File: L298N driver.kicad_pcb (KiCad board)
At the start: 2 copper layers, 155.6 x 80.8 mm, 32 parts, among them J2 Conn_01x02, J3 Conn_01x02, J6 Screw_Terminal_01x02, J8 Conn_01x02, J9 Conn_01x02, U1 L298N, U2 LM78M05_TO220, U3 DEV-15795, U4 74HC595, U5 L298N

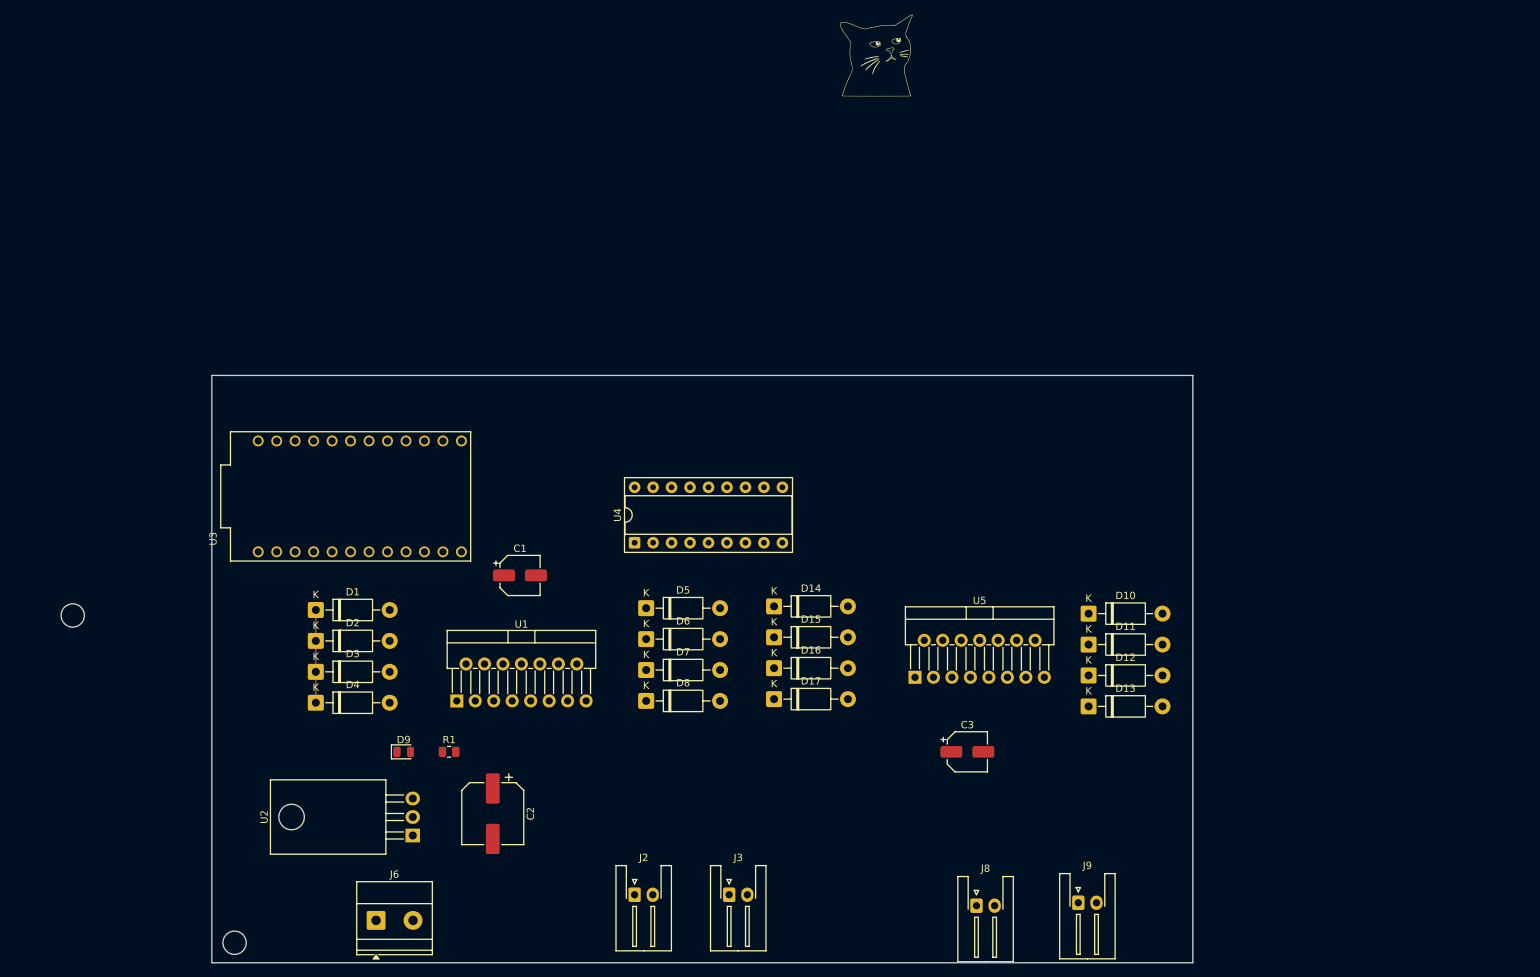
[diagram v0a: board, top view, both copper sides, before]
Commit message: changed to fast switching diode UF4004
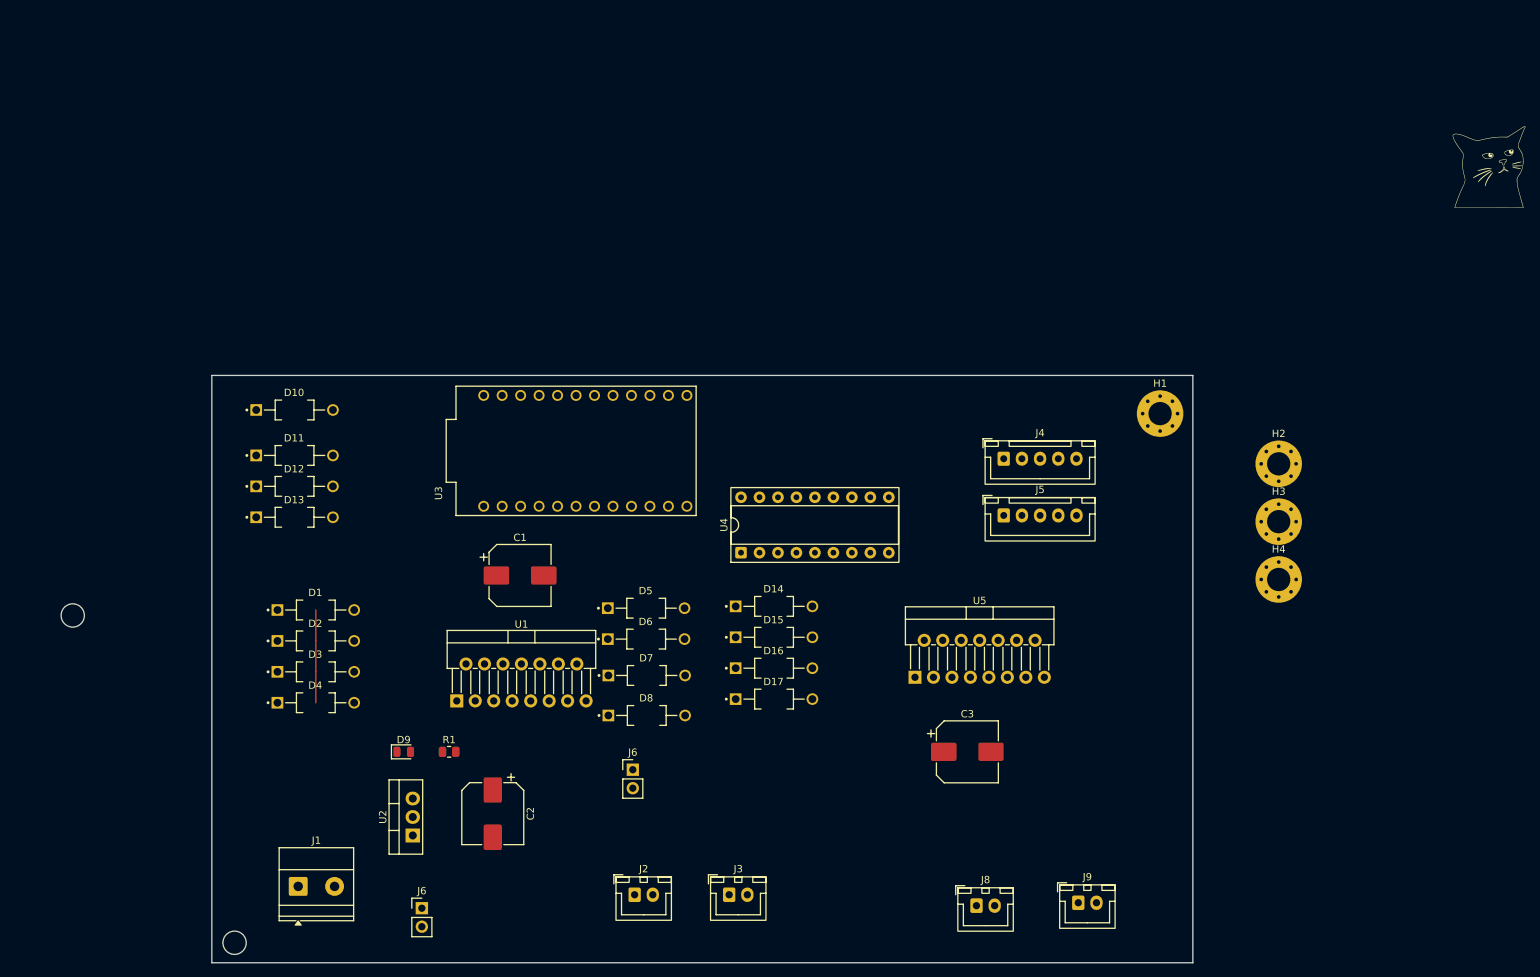
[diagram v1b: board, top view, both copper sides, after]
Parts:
- added H1: MountingHole, MountingHole:MountingHole_3.2mm_M3_Pad_Via, F.Cu at (189.0, 73.0)
- added H2: MountingHole, MountingHole:MountingHole_3.2mm_M3_Pad_Via, F.Cu at (205.3, 79.9)
- added H3: MountingHole, MountingHole:MountingHole_3.2mm_M3_Pad_Via, F.Cu at (205.3, 87.9)
- added H4: MountingHole, MountingHole:MountingHole_3.2mm_M3_Pad_Via, F.Cu at (205.3, 95.8)
- added J1: Screw_Terminal_01x03, TerminalBlock_Phoenix:TerminalBlock_Phoenix_MKDS-1,5-2_1x02_P5.00mm_Horizontal, F.Cu at (70.5, 138.0)
- added J4: Conn_01x05, Connector_JST:JST_XH_B5B-XH-A_1x05_P2.50mm_Vertical, F.Cu at (167.5, 79.2)
- added J5: Conn_01x05, Connector_JST:JST_XH_B5B-XH-A_1x05_P2.50mm_Vertical, F.Cu at (167.5, 87.0)
- added J6: Conn_01x02_Pin, Connector_PinHeader_2.54mm:PinHeader_1x02_P2.54mm_Vertical, F.Cu at (116.5, 122.0)
- C1, C3: value C_Polarized -> 220uF; footprint Capacitor_SMD:CP_Elec_5x4.4 -> Capacitor_SMD:CP_Elec_8x10
- C2: value C_Polarized -> 220uF; footprint Capacitor_SMD:CP_Elec_8x11.9 -> Capacitor_SMD:CP_Elec_8x10
- D1, D10, D11, D12, D13, D14, D15, D16, D17, D2, D3, D4, D5, D6, D7, D8: value 1N5819 -> UF4004; footprint Diode_THT:D_DO-41_SOD81_P10.16mm_Horizontal -> UF4004:DIOAD1055W87L533D272
- J2, J3, J8, J9: footprint Connector_JST:JST_XH_S2B-XH-A-1_1x02_P2.50mm_Horizontal -> Connector_JST:JST_XH_B2B-XH-A_1x02_P2.50mm_Vertical
- J6: value Screw_Terminal_01x02 -> Conn_01x02_Pin; footprint TerminalBlock_Phoenix:TerminalBlock_Phoenix_MKDS-1,5-2-5.08_1x02_P5.08mm_Horizontal -> Connector_PinHeader_2.54mm:PinHeader_1x02_P2.54mm_Vertical
- U2: footprint Package_TO_SOT_THT:TO-220-3_Horizontal_TabDown -> Package_TO_SOT_THT:TO-220-3_Vertical
- moved D10 112.7 mm to (70.0, 72.5)
- moved D11 112.2 mm to (70.0, 78.8)
- moved D12 112.2 mm to (70.0, 83.0)
- moved D13 112.2 mm to (70.0, 87.2)
- moved G*** 85.6 mm to (234.2, 39.1)
- moved U3 31.6 mm to (108.7, 78.1)
- moved U4 14.7 mm to (131.4, 92.1)
- moved J6 6.51 mm to (87.5, 141.0)
- moved D8 2.00 mm to (118.4, 114.5)
- moved D7 0.75 mm to (118.4, 109.0)
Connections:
- J2 pad 1: Net-(D1-A) -> Net-(J2-Pin_1)
- J2 pad 2: Net-(D2-A) -> Net-(J2-Pin_2)
- J3 pad 1: Net-(D3-A) -> Net-(J3-Pin_1)
- J3 pad 2: Net-(D4-A) -> Net-(J3-Pin_2)
- J6 pad 1: VCC -> /power
- J6 pad 2: /power -> VCC
- J8 pad 1: Net-(D10-A) -> Net-(J8-Pin_1)
- J8 pad 2: Net-(D12-A) -> Net-(J8-Pin_2)
- J9 pad 1: Net-(D14-A) -> Net-(J9-Pin_1)
- J9 pad 2: Net-(D16-A) -> Net-(J9-Pin_2)
- U1 pad 13: Net-(D3-A) -> Net-(J3-Pin_1)
- U1 pad 14: Net-(D4-A) -> Net-(J3-Pin_2)
- U1 pad 2: Net-(D1-A) -> Net-(J2-Pin_1)
- U1 pad 3: Net-(D2-A) -> Net-(J2-Pin_2)
- U5 pad 13: Net-(D14-A) -> Net-(J9-Pin_1)
- U5 pad 14: Net-(D16-A) -> Net-(J9-Pin_2)
- U5 pad 2: Net-(D10-A) -> Net-(J8-Pin_1)
- U5 pad 3: Net-(D12-A) -> Net-(J8-Pin_2)

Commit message: preliminary component placement and trace routing
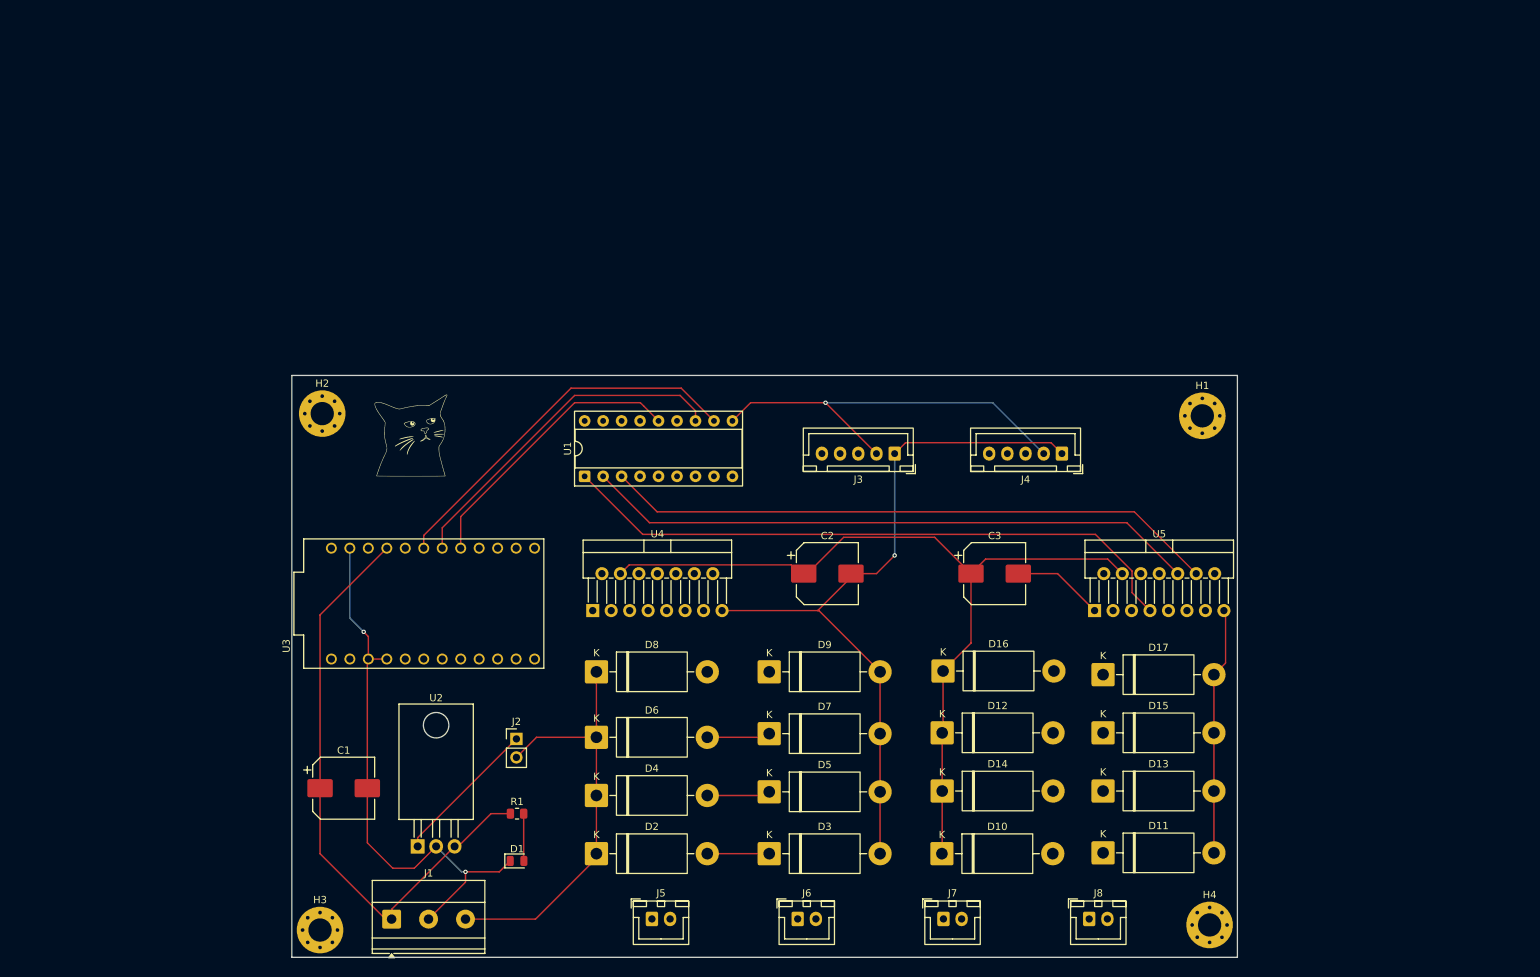
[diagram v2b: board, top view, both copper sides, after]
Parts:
- removed the J6 at (87.5, 141.0)
- removed the J6 at (116.5, 122.0)
- removed J9: Conn_01x02, Connector_JST:JST_XH_B2B-XH-A_1x02_P2.50mm_Vertical
- added J6: Conn_01x02, Connector_JST:JST_XH_B2B-XH-A_1x02_P2.50mm_Vertical, F.Cu at (139.2, 142.5)
- added J7: Conn_01x02, Connector_JST:JST_XH_B2B-XH-A_1x02_P2.50mm_Vertical, F.Cu at (159.2, 142.5)
- D1: value UF4004 -> LED; footprint UF4004:DIOAD1055W87L533D272 -> LED_SMD:LED_0805_2012Metric
- D10, D11, D12, D13, D14, D15, D16, D17, D2, D3, D4, D5, D6, D7, D8: value UF4004 -> UF5401; footprint UF4004:DIOAD1055W87L533D272 -> Diode_THT:D_DO-201AD_P15.24mm_Horizontal
- D9: value LED -> UF5401; footprint LED_SMD:LED_0805_2012Metric -> Diode_THT:D_DO-201AD_P15.24mm_Horizontal
- J1: footprint TerminalBlock_Phoenix:TerminalBlock_Phoenix_MKDS-1,5-2_1x02_P5.00mm_Horizontal -> TerminalBlock_Phoenix:TerminalBlock_Phoenix_MKDS-1,5-3-5.08_1x03_P5.08mm_Horizontal
- J2: value Conn_01x02 -> Conn_01x02_Pin; footprint Connector_JST:JST_XH_B2B-XH-A_1x02_P2.50mm_Vertical -> Connector_PinHeader_2.54mm:PinHeader_1x02_P2.54mm_Vertical
- J3: value Conn_01x02 -> Conn_01x05; footprint Connector_JST:JST_XH_B2B-XH-A_1x02_P2.50mm_Vertical -> Connector_JST:JST_XH_B5B-XH-A_1x05_P2.50mm_Vertical
- J5: value Conn_01x05 -> Conn_01x02; footprint Connector_JST:JST_XH_B5B-XH-A_1x05_P2.50mm_Vertical -> Connector_JST:JST_XH_B2B-XH-A_1x02_P2.50mm_Vertical
- U1: value L298N -> 74HC595; footprint Package_TO_SOT_THT:TO-220-15_P2.54x5.08mm_StaggerOdd_Lead4.58mm_Vertical -> Package_DIP:DIP-18_W7.62mm_Socket
- U2: footprint Package_TO_SOT_THT:TO-220-3_Vertical -> Package_TO_SOT_THT:TO-220-3_Horizontal_TabDown
- U4: value 74HC595 -> L298N; footprint Package_DIP:DIP-18_W7.62mm_Socket -> Package_TO_SOT_THT:TO-220-15_P2.54x5.08mm_StaggerOdd_Lead4.58mm_Vertical
- moved G*** 152.8 mm to (86.0, 76.0)
- moved H3 143.3 mm to (73.5, 144.0)
- moved H2 131.7 mm to (73.8, 73.0)
- moved D11 123.9 mm to (181.2, 133.4)
- moved D13 117.4 mm to (181.2, 124.9)
- moved D10 107.9 mm to (159.0, 133.5)
- moved D12 95.3 mm to (159.0, 116.9)
- moved J5 73.6 mm to (119.1, 142.5)
- moved D3 67.2 mm to (135.3, 133.5)
- moved J3 64.8 mm to (152.5, 78.5), turned to 180 degrees
- moved C2 56.6 mm to (143.2, 95.0), turned to 0 degrees
- moved D9 51.4 mm to (135.3, 108.5)
- moved H4 48.4 mm to (195.8, 143.3)
- moved D2 48.4 mm to (111.5, 133.5)
- moved D15 47.1 mm to (181.2, 116.9)
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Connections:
- C1 pad 1: VCC -> +5V
- C2 pad 1: +5V -> VCC
- D9 pad 1: GND -> Net-(D8-A)
- D9 pad 2: Net-(D9-A) -> GND
- J2 pad 1: Net-(J2-Pin_1) -> /power
- J2 pad 2: Net-(J2-Pin_2) -> VCC
- J3 pad 1: Net-(J3-Pin_1) -> GND
- J3 pad 2: Net-(J3-Pin_2) -> +5V
- J4 pad 4: /rotary_enc_roller_dt -> /rotary_enc_hydration_dt
- J4 pad 5: /rotary_enc_roller_clk -> /rotary_enc_hydration_clk
- J5 pad 1: GND -> Net-(D2-A)
- J5 pad 2: +5V -> Net-(D4-A)
- J8 pad 1: Net-(J8-Pin_1) -> Net-(D14-A)
- J8 pad 2: Net-(J8-Pin_2) -> Net-(D16-A)
- R1 pad 2: Net-(D9-A) -> Net-(D1-A)
- U1 pad 1: GND -> /roller_in2
- U1 pad 10: /hydration_in3 -> +5V
- U1 pad 11: /hydration_En -> /clk
- U1 pad 12: /hydration_in4 -> /latch
- U1 pad 13: Net-(J3-Pin_1) -> GND
- U1 pad 14: Net-(J3-Pin_2) -> /data
- U1 pad 15: GND -> /roller_in1
- U1 pad 2: Net-(J2-Pin_1) -> /hydration_in3
- U1 pad 3: Net-(J2-Pin_2) -> /hydration_in4
- U1 pad 4: VCC -> /extraction_in1
- U1 pad 5: /roller_in1 -> /extraction_in2
- U1 pad 6: /roller_En -> unconnected-(U1-QG-Pad6)
- U1 pad 7: /roller_in2 -> unconnected-(U1-QH-Pad7)
- U1 pad 9: +5V -> unconnected-(U1-QH'-Pad9)
- U4 pad 1: /roller_in2 -> GND
- U4 pad 10: +5V -> unconnected-(U4-IN3-Pad10)
- U4 pad 11: /clk -> unconnected-(U4-EnB-Pad11)
- U4 pad 12: /latch -> unconnected-(U4-IN4-Pad12)
- U4 pad 13: GND -> Net-(D6-A)
- U4 pad 14: /data -> Net-(D8-A)
- U4 pad 15: /roller_in1 -> GND
- U4 pad 2: /hydration_in3 -> Net-(D2-A)
- U4 pad 3: /hydration_in4 -> Net-(D4-A)
- U4 pad 4: /extraction_in1 -> VCC
- U4 pad 5: /extraction_in2 -> /extraction_in1
- U4 pad 6: unconnected-(U4-QG-Pad6) -> /extraction_En
- U4 pad 7: unconnected-(U4-QH-Pad7) -> /extraction_in2
- U4 pad 9: unconnected-(U4-QH'-Pad9) -> +5V
- U5 pad 10: unconnected-(U5-IN3-Pad10) -> /hydration_in3
- U5 pad 11: unconnected-(U5-EnB-Pad11) -> /hydration_En
- U5 pad 12: unconnected-(U5-IN4-Pad12) -> /hydration_in4
- U5 pad 13: Net-(J9-Pin_1) -> Net-(D14-A)
- U5 pad 14: Net-(J9-Pin_2) -> Net-(D16-A)
- U5 pad 2: Net-(J8-Pin_1) -> Net-(D10-A)
- U5 pad 3: Net-(J8-Pin_2) -> Net-(D12-A)
- U5 pad 5: /extraction_in1 -> /roller_in1
- U5 pad 6: /extraction_En -> /roller_En
- U5 pad 7: /extraction_in2 -> /roller_in2
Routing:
- net GND: track 0.00 -> 227.8 mm, vias 0 -> 3
- net VCC: track 12.8 -> 175.2 mm
- net +5V: track 0.00 -> 139.1 mm, vias 0 -> 1
- net /roller_in2: track 0.00 -> 87.1 mm
- net /hydration_in4: track 0.00 -> 84.5 mm
- net /hydration_in3: track 0.00 -> 84.5 mm
- net /clk: track 0.00 -> 51.9 mm
- net /latch: track 0.00 -> 47.4 mm
- net /data: track 0.00 -> 39.1 mm
- net /power: track 0.00 -> 20.4 mm
- net Net-(D6-A): track 0.00 -> 8.73 mm
- net Net-(D4-A): track 0.00 -> 8.73 mm
- net Net-(D2-A): track 0.00 -> 8.52 mm
- net Net-(D1-A): track 0.00 -> 6.51 mm
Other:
- board size 155.6 x 80.8 mm -> 130 x 80 mm

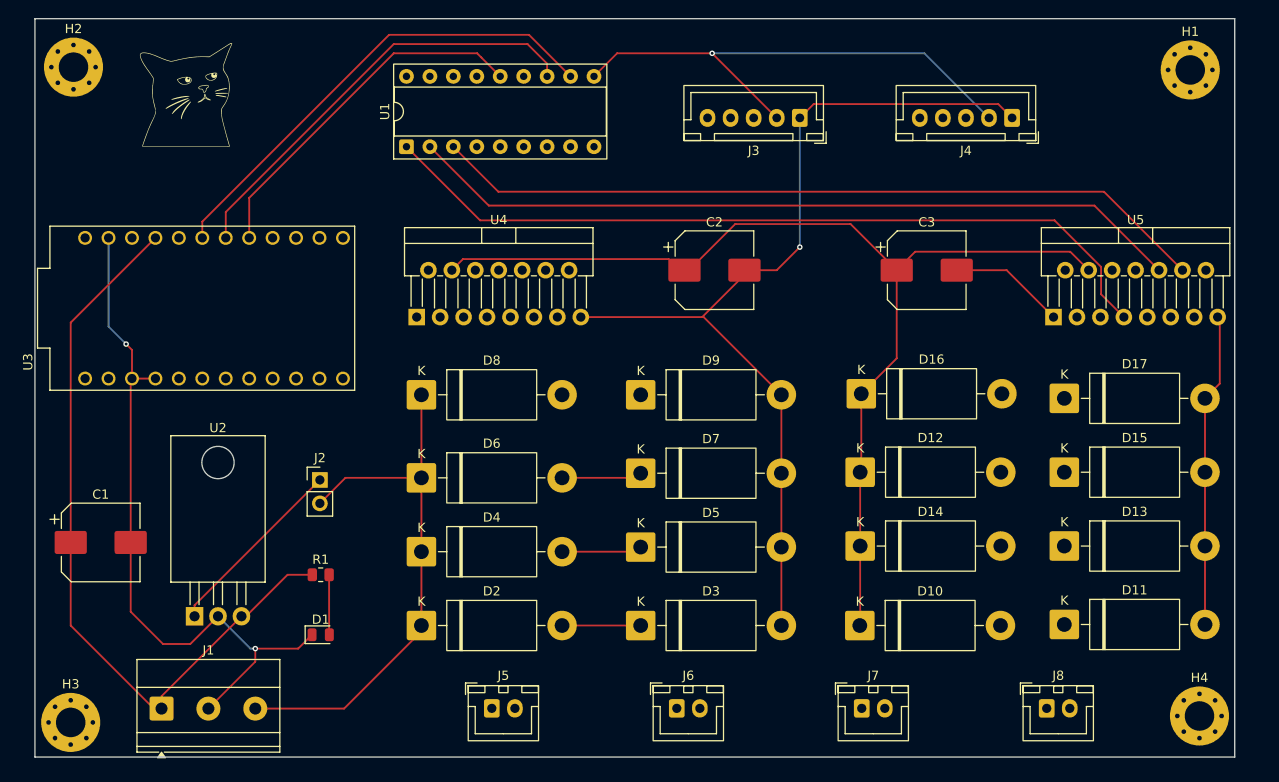
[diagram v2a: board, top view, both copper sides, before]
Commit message: finished preliminary routing
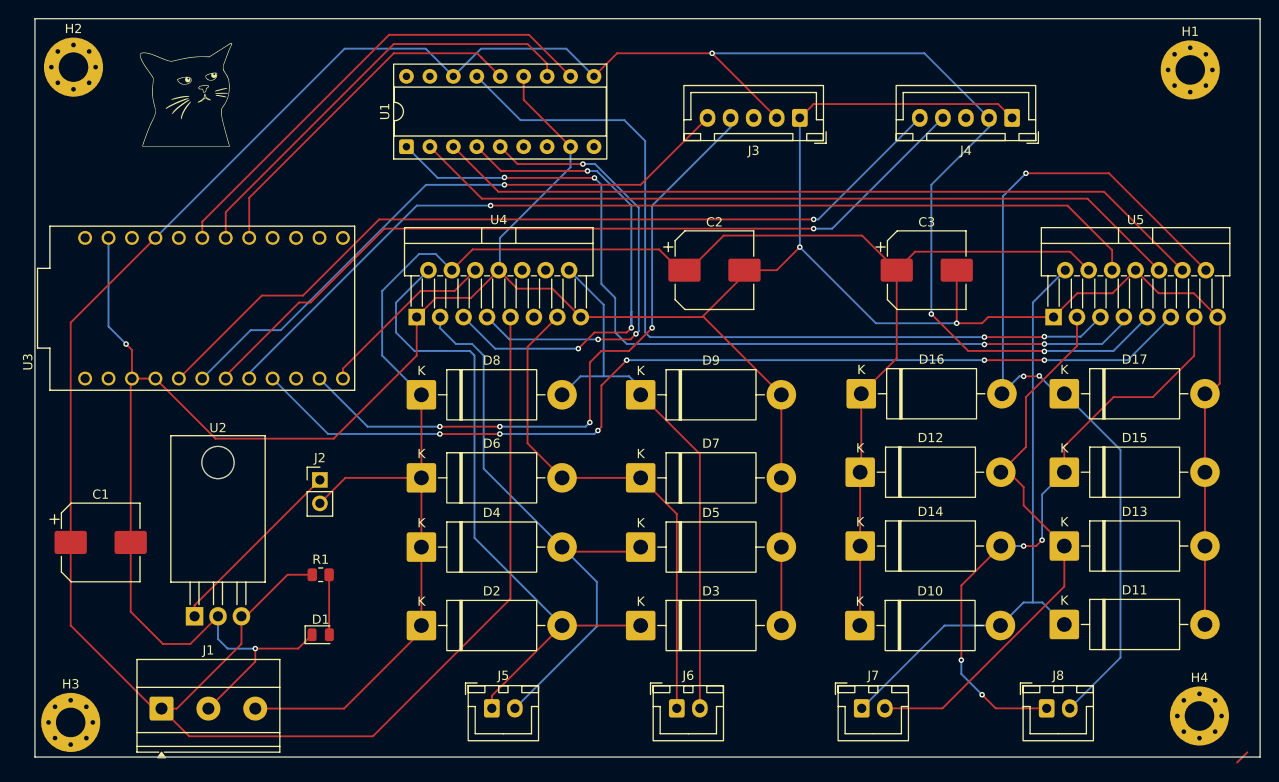
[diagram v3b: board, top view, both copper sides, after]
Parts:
- moved D17 0.50 mm to (181.2, 108.4)
- moved D4 0.50 mm to (111.5, 125.0)
- moved D7 0.50 mm to (135.3, 117.5)
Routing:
- net +5V: track 139.1 -> 326.0 mm, vias 1 -> 3
- net GND: track 227.8 -> 362.8 mm, vias 3 -> 4
- net /hydration_En: track 0.00 -> 108.2 mm, vias 0 -> 6
- net /roller_En: track 0.00 -> 105.8 mm, vias 0 -> 1
- net Net-(D16-A): track 0.00 -> 97.7 mm, vias 0 -> 3
- net /roller_in1: track 0.00 -> 92.3 mm, vias 0 -> 2
- net /rotary_enc_hydration_clk: track 0.00 -> 92.0 mm, vias 0 -> 1
- net /rotary_enc_hydration_dt: track 0.00 -> 89.6 mm, vias 0 -> 1
- net /rotary_enc_roller_dt: track 0.00 -> 72.7 mm, vias 0 -> 4
- net /rotary_enc_roller_clk: track 0.00 -> 66.4 mm, vias 0 -> 1
- net Net-(D10-A): track 0.00 -> 65.1 mm
- net Net-(D14-A): track 0.00 -> 64.8 mm, vias 0 -> 4
- net Net-(D2-A): track 8.52 -> 71.6 mm
- net Net-(D12-A): track 0.00 -> 60.9 mm
- net Net-(D8-A): track 0.00 -> 60.3 mm
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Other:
- board size 130 x 80 mm -> 132.8 x 80 mm
